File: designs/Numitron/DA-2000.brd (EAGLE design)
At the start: 59 x 98 mm, 13 parts, among them IC1 TLC5916IN, IC2 TLC5916IN, IC3 TLC5916IN, IC4 TLC5916IN

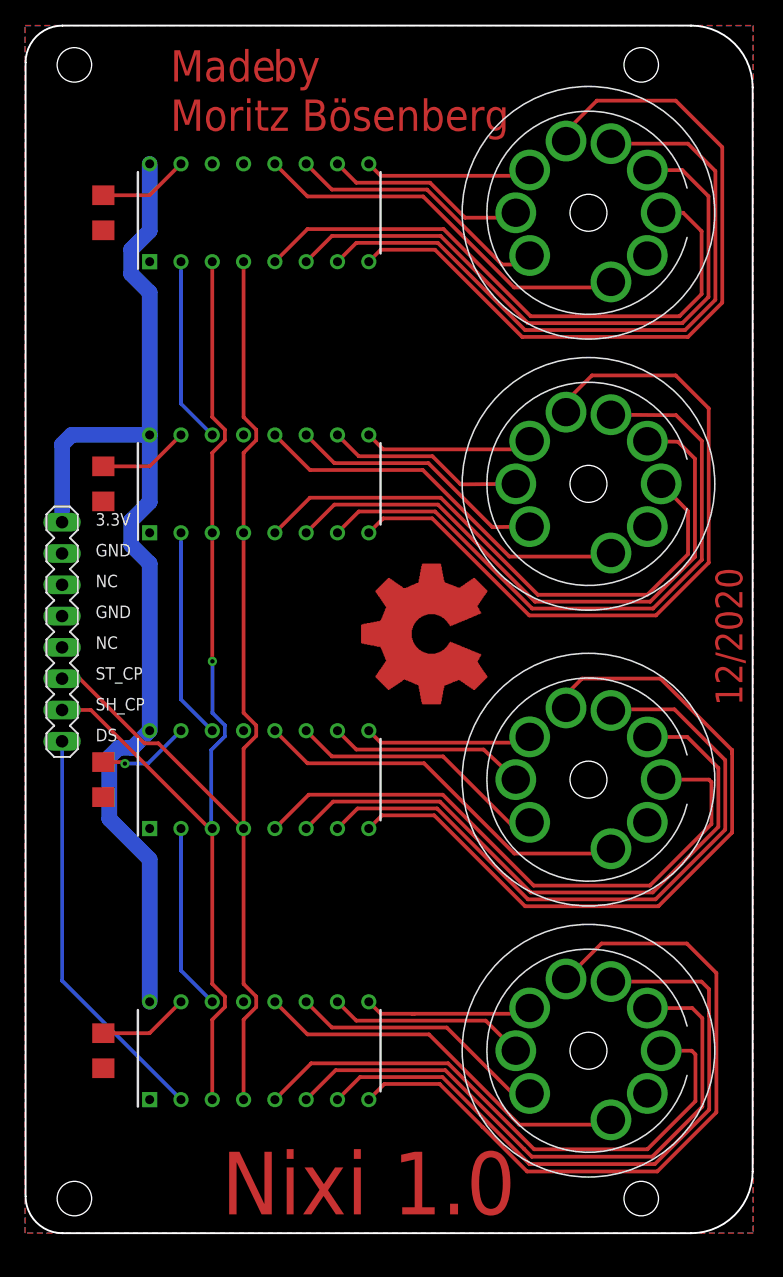
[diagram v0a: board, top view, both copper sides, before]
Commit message: changes for new design excluding swap for amplifier
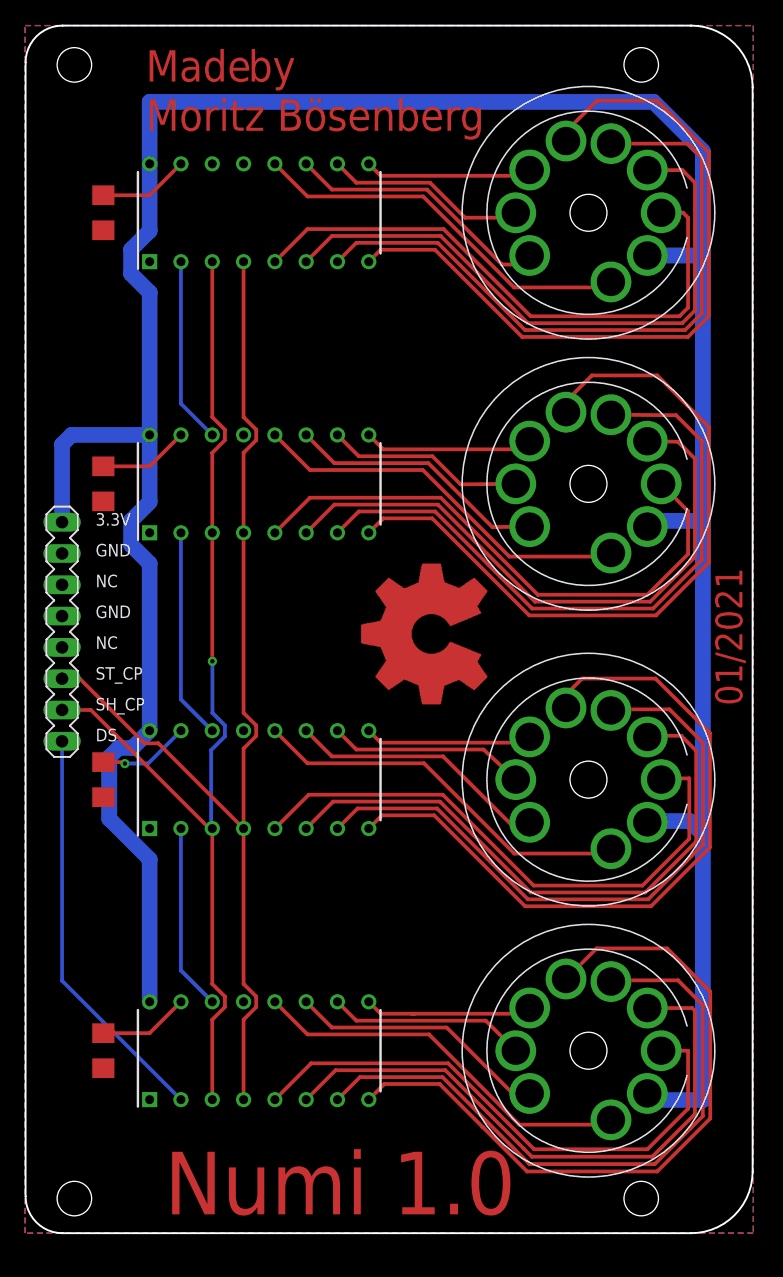
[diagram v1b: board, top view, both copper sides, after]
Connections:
- net 3.3V: now also U$1.2, U$2.2, U$3.2, U$4.2
- net GND: no longer U$1.2, U$2.2, U$3.2, U$4.2
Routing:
- net 3.3V: track 87.6 -> 235.3 mm
- net N$12: track 49.3 -> 46.6 mm
- net N$34: track 59.7 -> 57.6 mm
- net N$33: track 55.3 -> 53.2 mm
- net N$14: track 51.2 -> 49.2 mm
- net N$6: track 59.4 -> 57.4 mm
- net N$7: track 61.8 -> 60.1 mm
- net N$5: track 53.7 -> 52.3 mm
- net N$47: track 55.1 -> 54.2 mm
- net N$43: track 48.4 -> 47.5 mm
- net N$44: track 51.3 -> 50.4 mm
- net N$1: track 60.1 -> 59.2 mm
- net N$3: track 46.6 -> 45.9 mm
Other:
- board text added: "01/2021"
- board text added: "Numi 1.0"
- board text removed: "12/2020"
- board text removed: "Nixi 1.0"
